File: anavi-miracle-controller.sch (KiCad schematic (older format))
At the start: 23 parts, among them J1 Barrel_Jack_Switch, P1 CONN_01X03, SW1 SW_DIP_x01, T1 Screw_Terminal_01x06, U1 I2C_SENS_1, U2 I2C_SENS_1, U3 I2C_SENS_1, U4 Conn_01x04, U6 Conn_01x04

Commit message: Update schematics and PCB design
Major update to add SN74AHCT125D and to make the PCB design.

Signed-off-by: Leon Anavi <leon@anavi.org>
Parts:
- L1: footprint SOIC127P600X175-14N -> SN74AHCT125D:SOIC127P600X175-14N
- T1: footprint (none) -> TerminalBlock_Phoenix:TerminalBlock_Phoenix_MKDS-1,5-6_1x06_P5.00mm_Horizontal
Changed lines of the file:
@@
 F 0 "L1" H 4550 2270 50  0000 C CNN
 F 1 "SN74AHCT125D" H 4550 2179 50  0000 C CNN
-F 2 "SOIC127P600X175-14N" H 4550 1400 50  0001 L BNN
+F 2 "SN74AHCT125D:SOIC127P600X175-14N" H 4550 1400 50  0001 L BNN
 F 3 "SOIC-14 Texas Instruments" H 4550 1400 50  0001 L BNN
 F 4 "Buffer-line Driver 4 Channel Non-Inverting 3 State CMOS 14-Pin SOIC Tube" H 4550 1400 50  0001 L BNN "Field4"
@@
 F 0 "T1" H 9330 2742 50  0000 L CNN
 F 1 "Screw_Terminal_01x06" H 9330 2651 50  0000 L CNN
-F 2 "" H 9250 2750 50  0001 C CNN
+F 2 "TerminalBlock_Phoenix:TerminalBlock_Phoenix_MKDS-1,5-6_1x06_P5.00mm_Horizontal" H 9250 2750 50  0001 C CNN
 F 3 "~" H 9250 2750 50  0001 C CNN
 	1    9250 2750

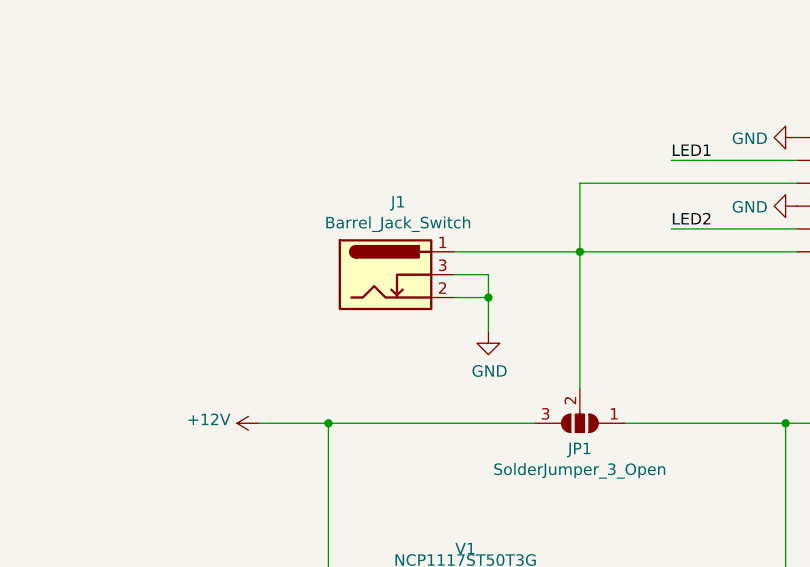
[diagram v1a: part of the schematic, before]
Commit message: Revision 1.1: Fix DC Jack
Update the schedatics, fix the DC jack on the PCB.

Signed-off-by: Leon Anavi <leon@anavi.org>
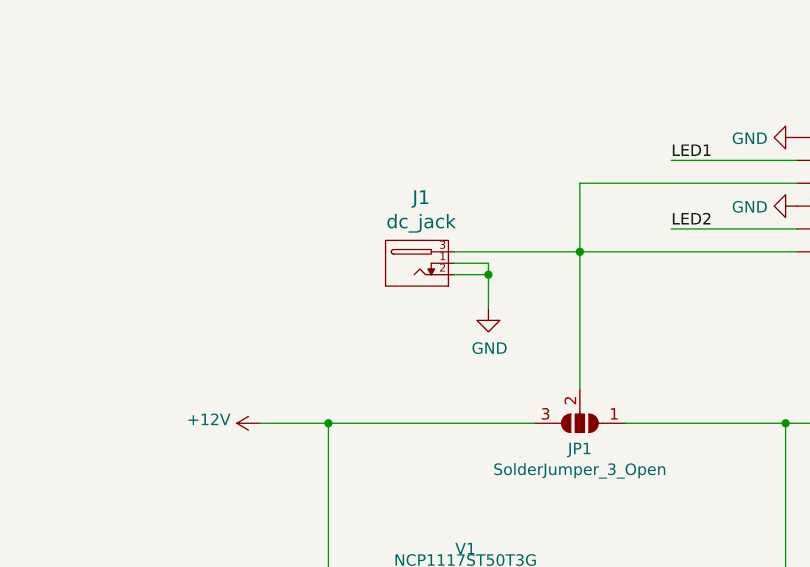
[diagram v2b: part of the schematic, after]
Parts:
- removed J1: Barrel_Jack_Switch, w_conn_misc:dc_socket, symbol Connector:Barrel_Jack_Switch
- added J1: dc_jack, w_conn_misc:dc_socket, symbol anavi-light-controller-rescue:dc_jack
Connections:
- net GND: now also J1.1, J1.2
- net at JP1.2 (C), T1.3 (Pin_3), T1.6 (Pin_6): now also J1.3
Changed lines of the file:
@@
-$EndComp
-$Comp
-L Connector:Barrel_Jack_Switch J1
-U 1 1 5CF338A0
-P 7250 3150
-F 0 "J1" H 7305 3467 50  0000 C CNN
-F 1 "Barrel_Jack_Switch" H 7305 3376 50  0000 C CNN
-F 2 "w_conn_misc:dc_socket" H 7300 3110 50  0001 C CNN
-F 3 "~" H 7300 3110 50  0001 C CNN
-	1    7250 3150
-	1    0    0    -1
 $EndComp
 $Comp
 L power:GND #PWR0106
 U 1 1 5CF33A2A
-P 7700 3400
-F 0 "#PWR0106" H 7700 3150 50  0001 C CNN
-F 1 "GND" H 7705 3227 50  0000 C CNN
-F 2 "" H 7700 3400 50  0001 C CNN
-F 3 "" H 7700 3400 50  0001 C CNN
-	1    7700 3400
+P 7700 3300
+F 0 "#PWR0106" H 7700 3050 50  0001 C CNN
+F 1 "GND" H 7705 3127 50  0000 C CNN
+F 2 "" H 7700 3300 50  0001 C CNN
+F 3 "" H 7700 3300 50  0001 C CNN
+	1    7700 3300
 	1    0    0    -1
 $EndComp
@@
 	7550 3150 7700 3150
 Wire Wire Line
-	7700 3150 7700 3250
-Wire Wire Line
-	7550 3250 7700 3250
-Connection ~ 7700 3250
-Wire Wire Line
-	7700 3250 7700 3400
+	7700 3150 7700 3300
 $Comp
 L anavi-miracle-controller-rescue:C-anavi-thermometer-rescue-anavi-gas-detector-rescue C1
@@
 Wire Wire Line
 	7900 3800 7000 3800
-Wire Wire Line
-	7550 3050 8100 3050
 Wire Wire Line
 	8100 3050 8100 3650
@@
 Wire Wire Line
 	7600 4900 7600 4850
+$Comp
+L anavi-light-controller-rescue:dc_jack J1
+U 1 1 5CFECCD1
+P 7400 3100
+F 0 "J1" H 7394 2813 60  0000 C CNN
+F 1 "dc_jack" H 7394 2919 60  0000 C CNN
+F 2 "w_conn_misc:dc_socket" H 7400 3100 60  0001 C CNN
+F 3 "" H 7400 3100 60  0000 C CNN
+	1    7400 3100
+	-1   0    0    1
+$EndComp
+Wire Wire Line
+	7550 3050 8100 3050
+Wire Wire Line
+	7550 3100 7700 3100
+Wire Wire Line
+	7700 3100 7700 3150
+Connection ~ 7700 3150
 $EndSCHEMATC
